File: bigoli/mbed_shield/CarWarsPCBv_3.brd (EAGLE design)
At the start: 68.6 x 55.9 mm, 28 parts, among them J1 MAGJACK, Q1 220mA/50V/3.5Ω, Q2 220mA/50V/3.5Ω, Q3 220mA/50V/3.5Ω, X1 E-STOP, X2 NEOPIXEL, X3 ENCODER, X4 POT, X5 STEER, X6 OSMC

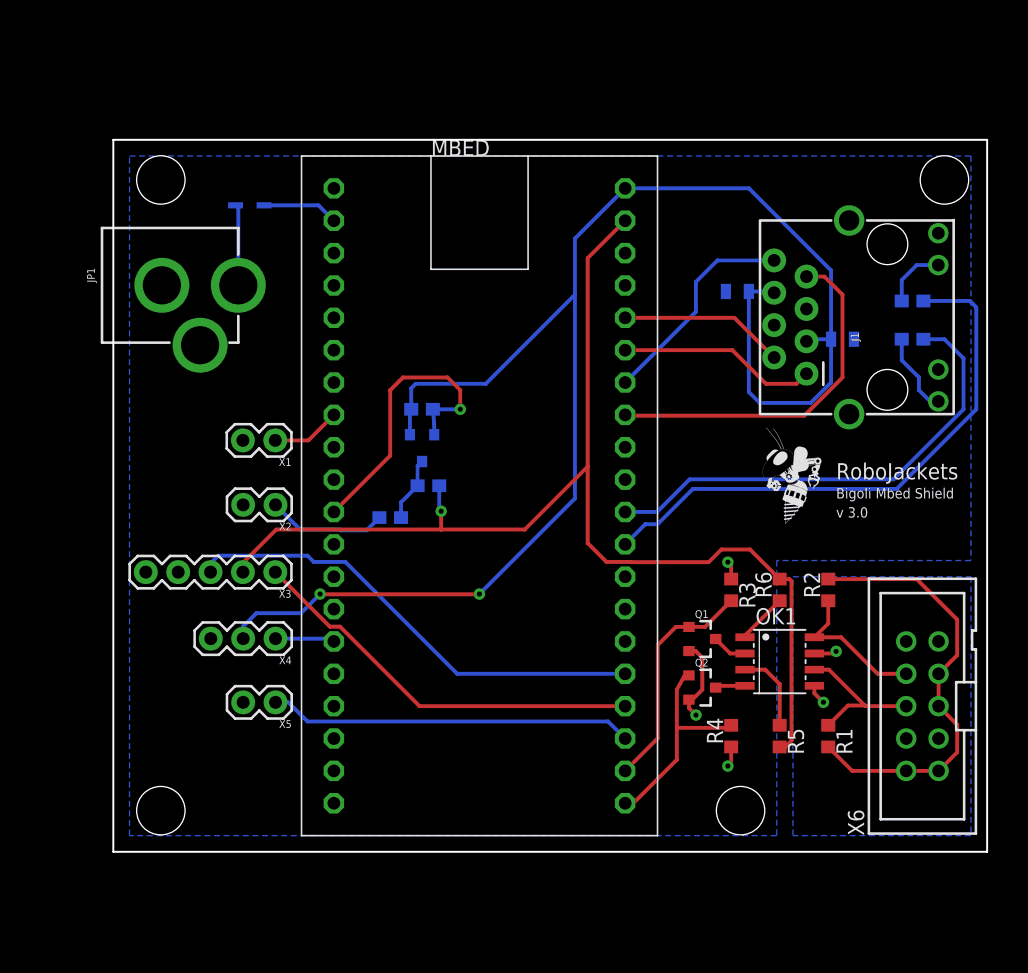
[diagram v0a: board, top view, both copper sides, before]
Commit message: Post Design Review of Bigoli Shield
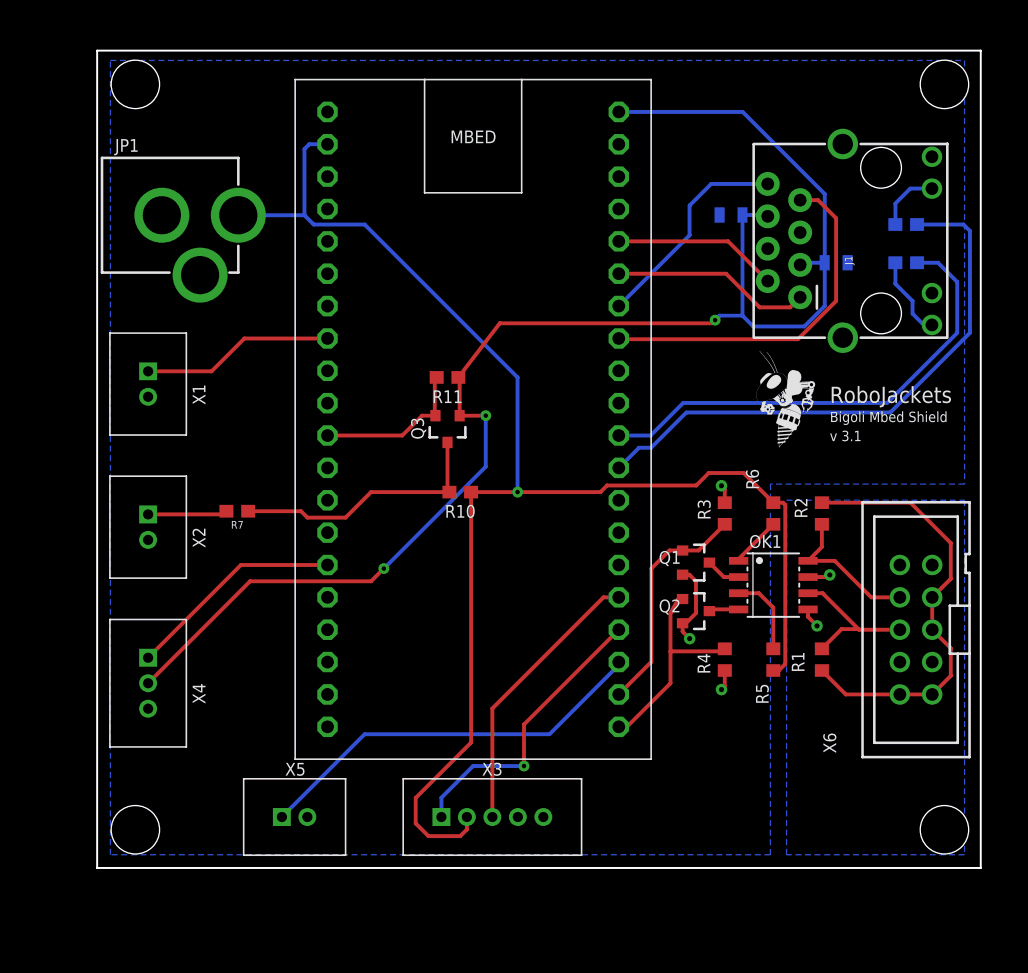
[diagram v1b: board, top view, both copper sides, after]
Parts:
- removed CR1: BAT60JFILM, Digikey:SOD-323
- Q1, Q2, Q3: value 220mA/50V/3.5Ω -> (none)
- X1, X2, X5: device SparkFun-Connectors:1X02 -> RoboJackets-Connectors:2MM-2-V
- X3: device SparkFun-Connectors:1X05 -> RoboJackets-Connectors:2MM-5-V
- X4: value POT -> STEER_POT; device SparkFun-Connectors:1X03 -> RoboJackets-Connectors:2MM-3-V
- moved X3 25.7 mm to (31.0, 4.00), turned to 0 degrees
- moved R7 12.0 mm to (11.0, 28.0), flipped to the top, turned to 180 degrees
- moved X1 10.9 mm to (4.00, 38.0), turned to 270 degrees
- moved X4 10.6 mm to (4.00, 14.5), turned to 270 degrees
- moved X2 10.2 mm to (4.00, 26.8), turned to 270 degrees
- moved X5 9.12 mm to (15.5, 4.00), turned to 0 degrees
- moved R1 6.02 mm to (56.9, 16.4)
- moved R4 6.02 mm to (49.3, 16.4)
- moved R5 6.02 mm to (53.1, 16.4)
- moved C1 6.02 mm to (49.8, 51.2)
- moved C2 6.02 mm to (58.0, 47.5)
- moved J1 6.02 mm to (72.6, 41.6)
- moved OK1 6.02 mm to (53.1, 22.2)
- moved Q1 6.02 mm to (47.0, 24.0)
- moved Q2 6.02 mm to (47.0, 20.2)
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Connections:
- removed net VCC: CR1.2, JP1.PWR
- removed net VIN: CR1.1, MBED.2
- net +5V: now also JP1.PWR, MBED.2; no longer MBED.39
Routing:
- net +5V: track 92.6 -> 116.7 mm
- net N$7: track 5.08 -> 20.8 mm
- net ENC_A: track 37.3 -> 22.1 mm
- net STEER_POT: track 4.67 -> 17.1 mm
- net NEOPIXEL_CONTROL: track 23.6 -> 12.2 mm, vias 1 -> 0
- net E-STOP_STATUS: track 5.43 -> 15.1 mm
- net +3V3: track 123.7 -> 114.3 mm, vias 2 -> 3
- net ENC_B: track 31.8 -> 22.8 mm, vias 0 -> 1
- net VCC: track 6.37 -> 0.00 mm
- net VIN: track 5.98 -> 0.00 mm
- net NEO_INPUT: track 9.39 -> 6.25 mm
- net STEER_PWM: track 28.6 -> 31.6 mm
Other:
- board size 68.6 x 55.9 mm -> 69.3 x 64.2 mm
- board text added: "v 3.1"
- board text removed: "v 3.0"

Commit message: Checked SeeedStudio design and fixed small routing issues
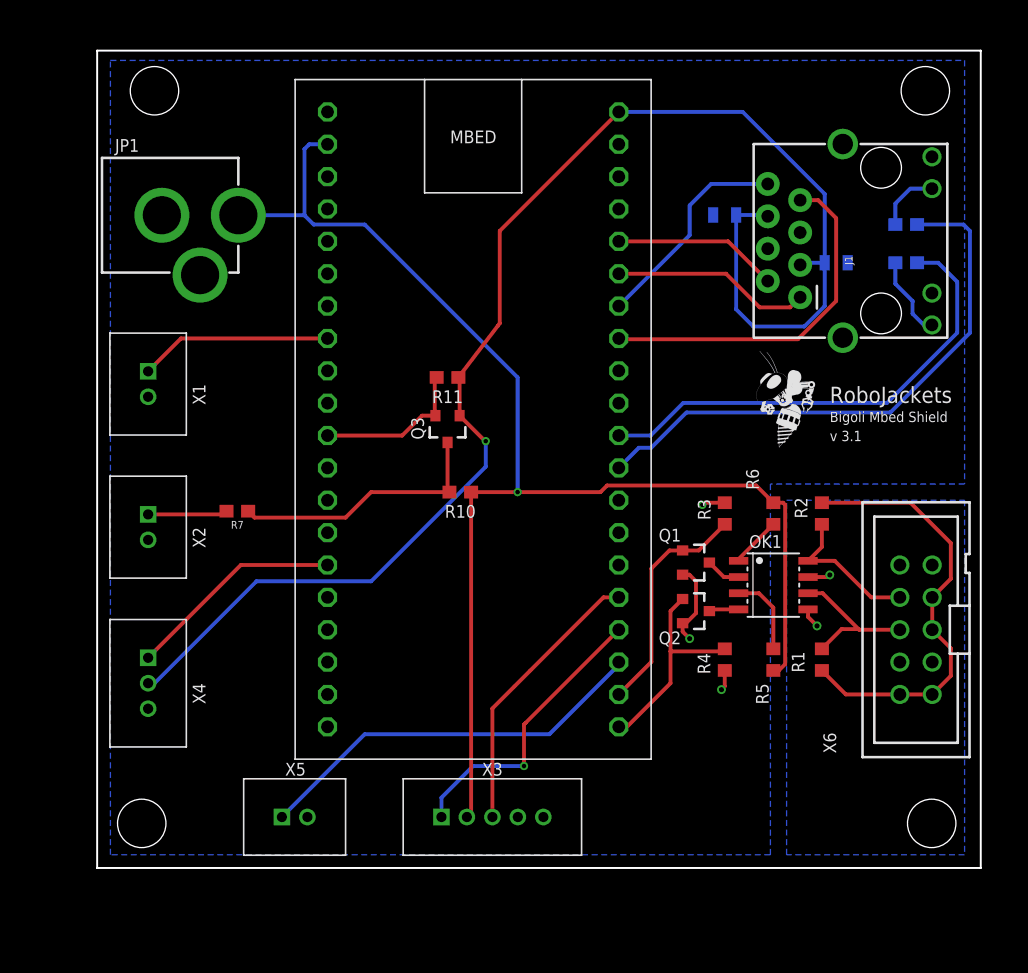
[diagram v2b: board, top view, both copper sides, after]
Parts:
- moved C1 0.50 mm to (49.2, 51.2)
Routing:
- net +5V: track 116.7 -> 108.1 mm
- net +3V3: track 114.3 -> 115.0 mm, vias 3 -> 1

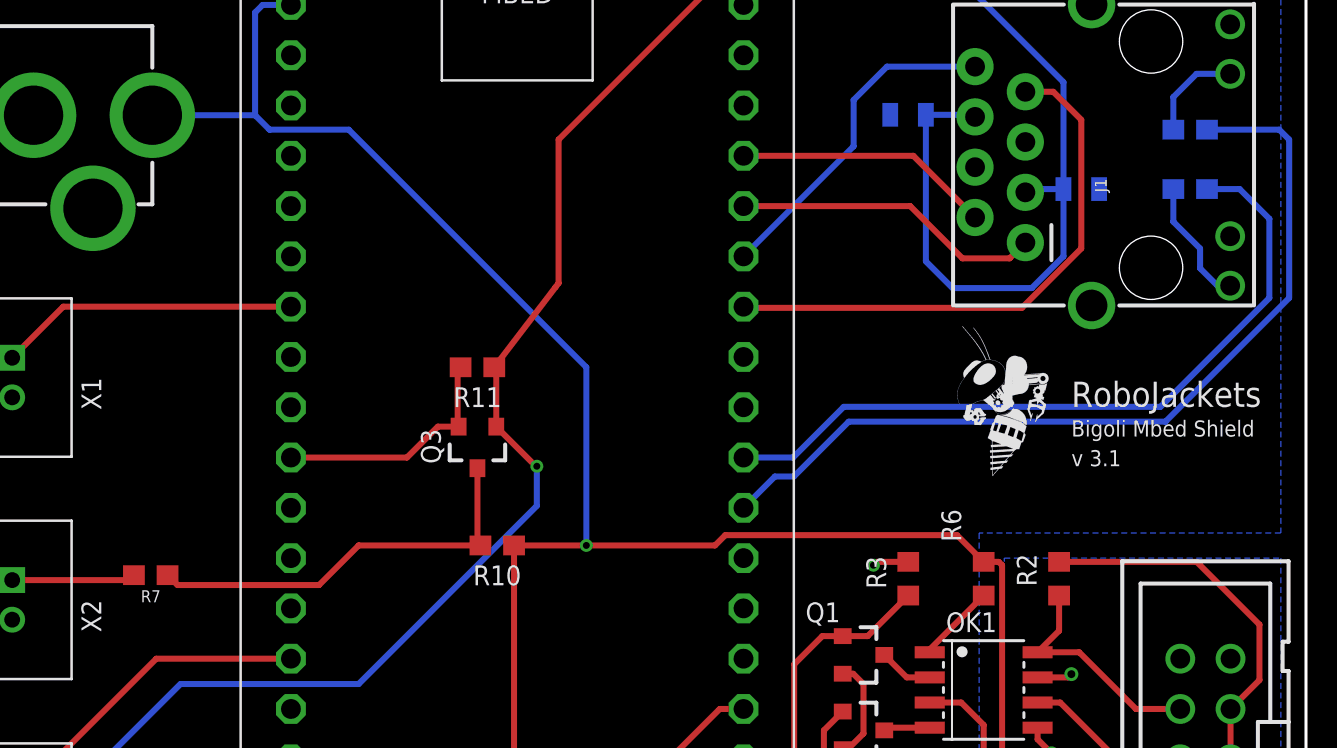
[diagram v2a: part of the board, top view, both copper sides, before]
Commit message: Created gerbers, changed resistor symbols
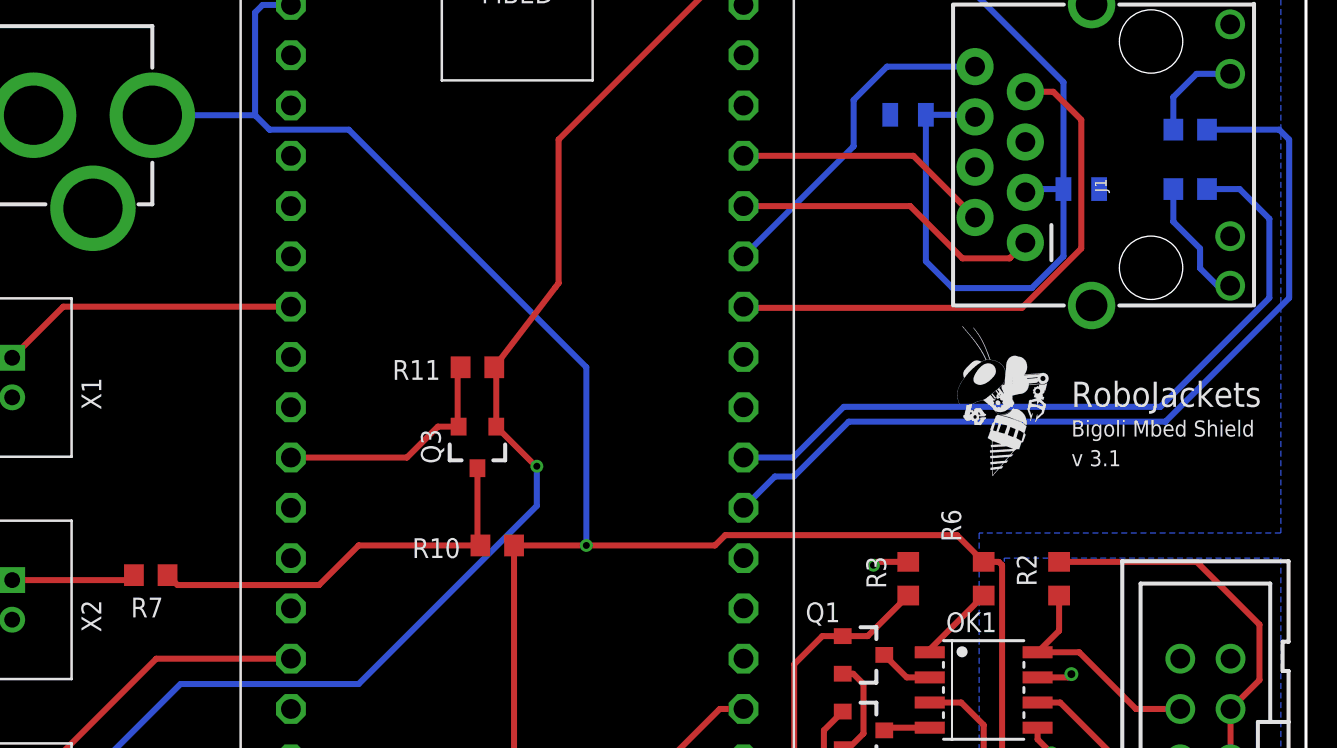
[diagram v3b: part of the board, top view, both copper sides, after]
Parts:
- R1, R2, R3, R4: value 10K -> 10k
- R10, R11: value 10K -> 10k; device SparkFun-Resistors:0603 -> rcl:R0603
- R5, R6: value 1K -> 1k
- R7, R8, R9: device SparkFun-Resistors:0603 -> rcl:R0603
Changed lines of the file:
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@@
 <attribute name="VALUE" x="46.95" y="18.509" size="0.6096" layer="27" font="vector" ratio="20" align="top-center"/>
 </element>
-<element name="R1" library="rcl" library_urn="urn:adsk.eagle:library:334" package="R0603" value="10K" x="56.88" y="16.35" smashed="yes" rot="R270">
+<element name="R1" library="rcl" library_urn="urn:adsk.eagle:library:334" package="R0603" package3d_urn="urn:adsk.eagle:package:23555/2" value="10k" x="56.88" y="16.35" smashed="yes" rot="R270">
 <attribute name="NAME" x="54.515" y="16.985" size="1" layer="25" rot="R270"/>
+<attribute name="SPICEPREFIX" value="R" x="56.88" y="16.35" size="1.778" layer="27" rot="R270" display="off"/>
 <attribute name="VALUE" x="58.225" y="17.235" size="1" layer="27" rot="R270"/>
 </element>
-<element name="R2" library="rcl" library_urn="urn:adsk.eagle:library:334" package="R0603" value="10K" x="56.88" y="27.82" smashed="yes" rot="R90">
+<element name="R2" library="rcl" library_urn="urn:adsk.eagle:library:334" package="R0603" package3d_urn="urn:adsk.eagle:package:23555/2" value="10k" x="56.88" y="27.82" smashed="yes" rot="R90">
 <attribute name="NAME" x="55.745" y="27.435" size="1" layer="25" rot="R90"/>
+<attribute name="SPICEPREFIX" value="R" x="56.88" y="27.82" size="1.778" layer="27" rot="R90" display="off"/>
 <attribute name="VALUE" x="59.285" y="27.185" size="1" layer="27" rot="R90"/>
 </element>
-<element name="R3" library="rcl" library_urn="urn:adsk.eagle:library:334" package="R0603" value="10K" x="49.26" y="27.82" smashed="yes" rot="R270">
+<element name="R3" library="rcl" library_urn="urn:adsk.eagle:library:334" package="R0603" package3d_urn="urn:adsk.eagle:package:23555/2" value="10k" x="49.26" y="27.82" smashed="yes" rot="R270">
 <attribute name="NAME" x="47.145" y="28.955" size="1" layer="25" rot="R270"/>
+<attribute name="SPICEPREFIX" value="R" x="49.26" y="27.82" size="1.778" layer="27" rot="R270" display="off"/>
 <attribute name="VALUE" x="50.355" y="29.455" size="1" layer="27" rot="R270"/>
 </element>
-<element name="R4" library="rcl" library_urn="urn:adsk.eagle:library:334" package="R0603" value="10K" x="49.26" y="16.35" smashed="yes" rot="R90">
+<element name="R4" library="rcl" library_urn="urn:adsk.eagle:library:334" package="R0603" package3d_urn="urn:adsk.eagle:package:23555/2" value="10k" x="49.26" y="16.35" smashed="yes" rot="R90">
 <attribute name="NAME" x="48.125" y="15.215" size="1" layer="25" rot="R90"/>
+<attribute name="SPICEPREFIX" value="R" x="49.26" y="16.35" size="1.778" layer="27" rot="R90" display="off"/>
 <attribute name="VALUE" x="50.335" y="17.285" size="1" layer="27" rot="R270"/>
 </element>
-<element name="R5" library="rcl" library_urn="urn:adsk.eagle:library:334" package="R0603" value="1K" x="53.07" y="16.35" smashed="yes" rot="R270">
+<element name="R5" library="rcl" library_urn="urn:adsk.eagle:library:334" package="R0603" package3d_urn="urn:adsk.eagle:package:23555/2" value="1k" x="53.07" y="16.35" smashed="yes" rot="R270">
 <attribute name="NAME" x="51.705" y="14.485" size="1" layer="25" rot="R270"/>
+<attribute name="SPICEPREFIX" value="R" x="53.07" y="16.35" size="1.778" layer="27" rot="R270" display="off"/>
 <attribute name="VALUE" x="53.665" y="14.485" size="1" layer="27" rot="R270"/>
 </element>
-<element name="R6" library="rcl" library_urn="urn:adsk.eagle:library:334" package="R0603" value="1K" x="53.07" y="27.82" smashed="yes" rot="R90">
+<element name="R6" library="rcl" library_urn="urn:adsk.eagle:library:334" package="R0603" package3d_urn="urn:adsk.eagle:package:23555/2" value="1k" x="53.07" y="27.82" smashed="yes" rot="R90">
 <attribute name="NAME" x="51.935" y="29.685" size="1" layer="25" rot="R90"/>
+<attribute name="SPICEPREFIX" value="R" x="53.07" y="27.82" size="1.778" layer="27" rot="R90" display="off"/>
 <attribute name="VALUE" x="54.475" y="29.935" size="1" layer="27" rot="R90"/>
 </element>
-<element name="R7" library="SparkFun-Resistors" library_urn="urn:adsk.eagle:library:532" package="0603" package3d_urn="urn:adsk.eagle:package:39650/1" value="340" x="11" y="28" rot="R180">
-<attribute name="PROD_ID" value="RES-12616" x="11" y="28" size="1.778" layer="27" rot="R180" display="off"/>
+<element name="R7" library="rcl" library_urn="urn:adsk.eagle:library:334" package="R0603" package3d_urn="urn:adsk.eagle:package:23555/2" value="340" x="11" y="28" smashed="yes" rot="R180">
+<attribute name="NAME" x="11.635" y="26.865" size="1" layer="25" rot="R180"/>
+<attribute name="SPICEPREFIX" value="R" x="11" y="28" size="1.778" layer="27" rot="R180" display="off"/>
+<attribute name="VALUE" x="12.135" y="30.405" size="1" layer="27" rot="R180"/>
 </element>
 <element name="X2" library="RoboJackets-Connectors" package="2MM-2-V" value="NEOPIXEL" x="4" y="26.75" smashed="yes" rot="R270">
@@
 <attribute name="VALUE" x="56.984" y="49.897" size="1" layer="28" rot="MR180"/>
 </element>
-<element name="R8" library="SparkFun-Resistors" library_urn="urn:adsk.eagle:library:532" package="0603" package3d_urn="urn:adsk.eagle:package:39650/1" value="47" x="63.5" y="47.5" smashed="yes" rot="MR180">
-<attribute name="NAME" x="62.5" y="49.488" size="1" layer="26" font="vector" ratio="20" rot="MR180" align="bottom-center"/>
-<attribute name="PROD_ID" value="RES-12616" x="63.5" y="47.5" size="1.778" layer="28" rot="MR180" display="off"/>
-<attribute name="VALUE" x="64.75" y="48.512" size="1" layer="28" font="vector" ratio="20" rot="MR180" align="top-center"/>
+<element name="R8" library="rcl" library_urn="urn:adsk.eagle:library:334" package="R0603" package3d_urn="urn:adsk.eagle:package:23555/2" value="47" x="63.5" y="47.5" smashed="yes" rot="MR180">
+<attribute name="NAME" x="59.865" y="47.865" size="1" layer="26" rot="MR180"/>
+<attribute name="SPICEPREFIX" value="R" x="63.5" y="47.5" size="1.778" layer="28" rot="MR180" display="off"/>
+<attribute name="VALUE" x="65.365" y="47.905" size="1" layer="28" rot="MR180"/>
 </element>
-<element name="R9" library="SparkFun-Resistors" library_urn="urn:adsk.eagle:library:532" package="0603" package3d_urn="urn:adsk.eagle:package:39650/1" value="47" x="63.5" y="50.5" smashed="yes" rot="MR180">
-<attribute name="NAME" x="62.5" y="52.488" size="1" layer="26" font="vector" ratio="20" rot="MR180" align="bottom-center"/>
-<attribute name="PROD_ID" value="RES-12616" x="63.5" y="50.5" size="1.778" layer="28" rot="MR180" display="off"/>
-<attribute name="VALUE" x="64.75" y="51.512" size="1" layer="28" font="vector" ratio="20" rot="MR180" align="top-center"/>
+<element name="R9" library="rcl" library_urn="urn:adsk.eagle:library:334" package="R0603" package3d_urn="urn:adsk.eagle:package:23555/2" value="47" x="63.5" y="50.5" smashed="yes" rot="MR180">
+<attribute name="NAME" x="59.865" y="50.865" size="1" layer="26" rot="MR180"/>
+<attribute name="SPICEPREFIX" value="R" x="63.5" y="50.5" size="1.778" layer="28" rot="MR180" display="off"/>
+<attribute name="VALUE" x="65.365" y="50.905" size="1" layer="28" rot="MR180"/>
 </element>
 <element name="X5" library="RoboJackets-Connectors" package="2MM-2-V" value="STEER" x="15.5" y="4" smashed="yes">
@@
 <attribute name="VALUE" x="25.849" y="34.5" size="1" layer="27" font="vector" ratio="20" rot="R270" align="top-center"/>
 </element>
-<element name="R10" library="SparkFun-Resistors" library_urn="urn:adsk.eagle:library:532" package="0603" package3d_urn="urn:adsk.eagle:package:39650/1" value="10K" x="28.5" y="29.5" smashed="yes" rot="R180">
-<attribute name="NAME" x="28.5" y="28.488" size="1" layer="25" font="vector" ratio="20" rot="R180" align="bottom-center"/>
-<attribute name="PROD_ID" value="RES-12616" x="28.5" y="29.5" size="1.778" layer="27" rot="R180" display="off"/>
-<attribute name="VALUE" x="28.5" y="30.512" size="1" layer="27" font="vector" ratio="20" rot="R180" align="top-center"/>
+<element name="R10" library="rcl" library_urn="urn:adsk.eagle:library:334" package="R0603" package3d_urn="urn:adsk.eagle:package:23555/2" value="10k" x="28.5" y="29.5" smashed="yes" rot="R180">
+<attribute name="NAME" x="26.635" y="29.865" size="1" layer="25" rot="R180"/>
+<attribute name="SPICEPREFIX" value="R" x="28.5" y="29.5" size="1.778" layer="27" rot="R180" display="off"/>
+<attribute name="VALUE" x="29.635" y="31.905" size="1" layer="27" rot="R180"/>
 </element>
-<element name="R11" library="SparkFun-Resistors" library_urn="urn:adsk.eagle:library:532" package="0603" package3d_urn="urn:adsk.eagle:package:39650/1" value="10K" x="27.5" y="38.5" smashed="yes" rot="R180">
-<attribute name="NAME" x="27.5" y="37.488" size="1" layer="25" font="vector" ratio="20" rot="R180" align="bottom-center"/>
-<attribute name="PROD_ID" value="RES-12616" x="27.5" y="38.5" size="1.778" layer="27" rot="R180" display="off"/>
-<attribute name="VALUE" x="27.5" y="39.512" size="1" layer="27" font="vector" ratio="20" rot="R180" align="top-center"/>
+<element name="R11" library="rcl" library_urn="urn:adsk.eagle:library:334" package="R0603" package3d_urn="urn:adsk.eagle:package:23555/2" value="10k" x="27.5" y="38.5" smashed="yes" rot="R180">
+<attribute name="NAME" x="25.635" y="38.865" size="1" layer="25" rot="R180"/>
+<attribute name="SPICEPREFIX" value="R" x="27.5" y="38.5" size="1.778" layer="27" rot="R180" display="off"/>
+<attribute name="VALUE" x="28.135" y="40.905" size="1" layer="27" rot="R180"/>
 </element>
 <element name="X4" library="RoboJackets-Connectors" package="2MM-3-V" value="STEER_POT" x="4" y="14.5" smashed="yes" rot="R270">
